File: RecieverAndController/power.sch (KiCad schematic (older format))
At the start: 4 parts

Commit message: did easy stuff
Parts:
- removed C?: 1uF, symbol C
- removed U?: AP2204_5V, symbol AP2204
- U?: value AP2204_5V -> AP2204_3V3
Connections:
- net labels removed: +BATT
- wire segments 6 -> 3
- no-connect marks 2 -> 1
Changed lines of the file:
@@
-$Comp
-L C C?
-U 1 1 5A9AC800
-P 1800 2200
-F 0 "C?" H 1825 2300 50  0000 L CNN
-F 1 "1uF" H 1825 2100 50  0000 L CNN
-F 2 "" H 1838 2050 50  0001 C CNN
-F 3 "" H 1800 2200 50  0001 C CNN
-	1    1800 2200
-	1    0    0    -1
-$EndComp
-$Comp
-L GND #PWR?
-U 1 1 5A9ACF4F
-P 1800 2350
-F 0 "#PWR?" H 1800 2100 50  0001 C CNN
-F 1 "GND" H 1800 2200 50  0000 C CNN
-F 2 "" H 1800 2350 50  0001 C CNN
-F 3 "" H 1800 2350 50  0001 C CNN
-	1    1800 2350
-	1    0    0    -1
-$EndComp
-$Comp
-L +BATT #PWR?
-U 1 1 5A9ACF69
-P 1800 2050
-F 0 "#PWR?" H 1800 1900 50  0001 C CNN
-F 1 "+BATT" H 1800 2190 50  0000 C CNN
-F 2 "" H 1800 2050 50  0001 C CNN
-F 3 "" H 1800 2050 50  0001 C CNN
-	1    1800 2050
-	1    0    0    -1
-$EndComp
-$Comp
-L +5V #PWR?
-U 1 1 5A9AD015
-P 3200 2050
-F 0 "#PWR?" H 3200 1900 50  0001 C CNN
-F 1 "+5V" H 3200 2190 50  0000 C CNN
-F 2 "" H 3200 2050 50  0001 C CNN
-F 3 "" H 3200 2050 50  0001 C CNN
-	1    3200 2050
-	1    0    0    -1
-$EndComp
-Wire Wire Line
-	2100 2300 2100 2050
-Wire Wire Line
-	2100 2050 1800 2050
-Wire Wire Line
-	2900 2050 3200 2050
-NoConn ~ 2900 2300
-$Comp
-L AP2204 U?
-U 1 1 5A9AD312
-P 2500 2200
-F 0 "U?" H 2500 2200 60  0000 C CNN
-F 1 "AP2204_5V" H 2500 2650 60  0000 C CNN
-F 2 "" H 2500 2200 60  0001 C CNN
-F 3 "" H 2500 2200 60  0001 C CNN
-	1    2500 2200
-	1    0    0    -1
-$EndComp
-$Comp
-L GND #PWR?
-U 1 1 5A9AD3A9
-P 2500 2850
-F 0 "#PWR?" H 2500 2600 50  0001 C CNN
-F 1 "GND" H 2500 2700 50  0000 C CNN
-F 2 "" H 2500 2850 50  0001 C CNN
-F 3 "" H 2500 2850 50  0001 C CNN
-	1    2500 2850
-	1    0    0    -1
-$EndComp
 $Comp
 L C C?
@@
 	1    0    0    -1
 $EndComp
-$Comp
-L +BATT #PWR?
-U 1 1 5A9AD453
-P 3550 2050
-F 0 "#PWR?" H 3550 1900 50  0001 C CNN
-F 1 "+BATT" H 3550 2190 50  0000 C CNN
-F 2 "" H 3550 2050 50  0001 C CNN
-F 3 "" H 3550 2050 50  0001 C CNN
-	1    3550 2050
-	1    0    0    -1
-$EndComp
 Wire Wire Line
 	3850 2300 3850 2050
@@
 P 4250 2200
 F 0 "U?" H 4250 2200 60  0000 C CNN
-F 1 "AP2204_5V" H 4250 2650 60  0000 C CNN
+F 1 "AP2204_3V3" H 4250 2650 60  0000 C CNN
 F 2 "" H 4250 2200 60  0001 C CNN
 F 3 "" H 4250 2200 60  0001 C CNN
@@
 	1    0    0    -1
 $EndComp
+$Comp
+L +5V #PWR?
+U 1 1 5ACA0F2D
+P 3550 2050
+F 0 "#PWR?" H 3550 1900 50  0001 C CNN
+F 1 "+5V" H 3550 2190 50  0000 C CNN
+F 2 "" H 3550 2050 50  0001 C CNN
+F 3 "" H 3550 2050 50  0001 C CNN
+	1    3550 2050
+	1    0    0    -1
+$EndComp

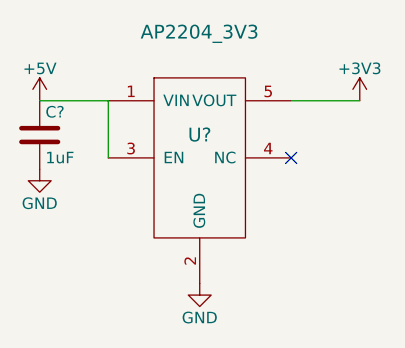
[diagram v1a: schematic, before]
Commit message: adding footprints to schematic
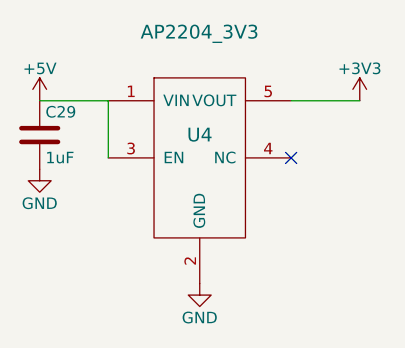
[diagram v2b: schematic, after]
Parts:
- C29: renamed from C?; footprint (none) -> Capacitors_SMD:C_0603
- U4: renamed from U?; footprint (none) -> TO_SOT_Packages_SMD:SOT-23-5
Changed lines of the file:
@@
 $EndDescr
 $Comp
-L C C?
+L C C29
 U 1 1 5A9AD447
 P 3550 2200
-F 0 "C?" H 3575 2300 50  0000 L CNN
+F 0 "C29" H 3575 2300 50  0000 L CNN
 F 1 "1uF" H 3575 2100 50  0000 L CNN
-F 2 "" H 3588 2050 50  0001 C CNN
+F 2 "Capacitors_SMD:C_0603" H 3588 2050 50  0001 C CNN
 F 3 "" H 3550 2200 50  0001 C CNN
 	1    3550 2200
@@
 $EndComp
 $Comp
-L GND #PWR?
+L GND #PWR035
 U 1 1 5A9AD44D
 P 3550 2350
-F 0 "#PWR?" H 3550 2100 50  0001 C CNN
+F 0 "#PWR035" H 3550 2100 50  0001 C CNN
 F 1 "GND" H 3550 2200 50  0000 C CNN
 F 2 "" H 3550 2350 50  0001 C CNN
@@
 NoConn ~ 4650 2300
 $Comp
-L AP2204 U?
+L AP2204 U4
 U 1 1 5A9AD463
 P 4250 2200
-F 0 "U?" H 4250 2200 60  0000 C CNN
+F 0 "U4" H 4250 2200 60  0000 C CNN
 F 1 "AP2204_3V3" H 4250 2650 60  0000 C CNN
-F 2 "" H 4250 2200 60  0001 C CNN
+F 2 "TO_SOT_Packages_SMD:SOT-23-5" H 4250 2200 60  0001 C CNN
 F 3 "" H 4250 2200 60  0001 C CNN
 	1    4250 2200
@@
 $EndComp
 $Comp
-L GND #PWR?
+L GND #PWR036
 U 1 1 5A9AD469
 P 4250 2850
-F 0 "#PWR?" H 4250 2600 50  0001 C CNN
+F 0 "#PWR036" H 4250 2600 50  0001 C CNN
 F 1 "GND" H 4250 2700 50  0000 C CNN
 F 2 "" H 4250 2850 50  0001 C CNN
@@
 $EndComp
 $Comp
-L +3V3 #PWR?
+L +3V3 #PWR037
 U 1 1 5A9AD4F2
 P 4950 2050
-F 0 "#PWR?" H 4950 1900 50  0001 C CNN
+F 0 "#PWR037" H 4950 1900 50  0001 C CNN
 F 1 "+3V3" H 4950 2190 50  0000 C CNN
 F 2 "" H 4950 2050 50  0001 C CNN
@@
 $EndComp
 $Comp
-L +5V #PWR?
+L +5V #PWR038
 U 1 1 5ACA0F2D
 P 3550 2050
-F 0 "#PWR?" H 3550 1900 50  0001 C CNN
+F 0 "#PWR038" H 3550 1900 50  0001 C CNN
 F 1 "+5V" H 3550 2190 50  0000 C CNN
 F 2 "" H 3550 2050 50  0001 C CNN
